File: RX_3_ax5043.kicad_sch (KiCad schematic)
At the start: 32 parts, among them U401 RFShield_OnePiece, U405 AX5043, U406 TPS22919D

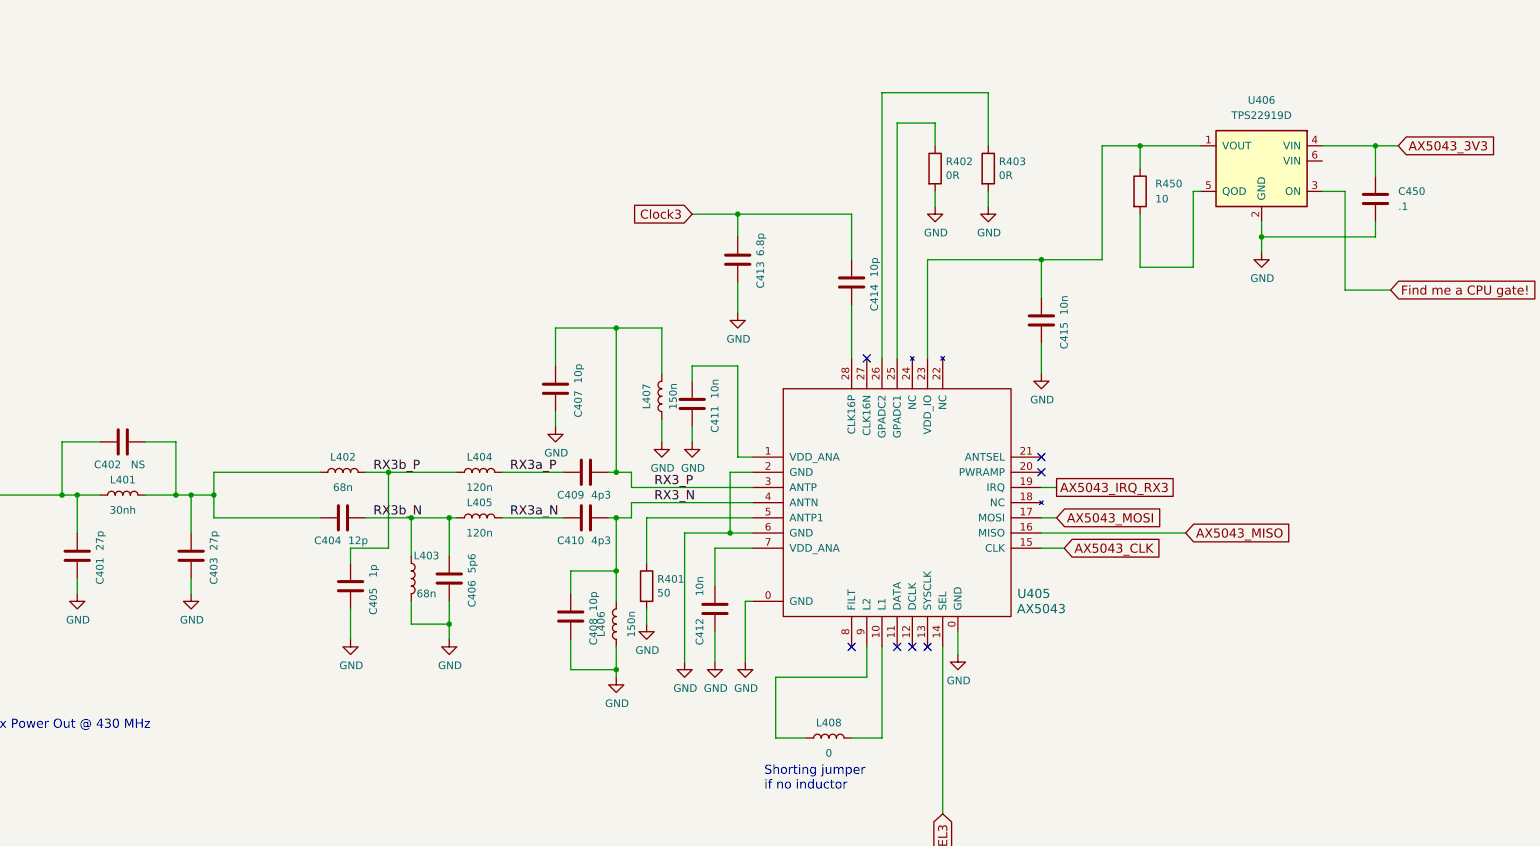
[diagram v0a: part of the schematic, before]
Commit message: Lots of cleanups to fix numerous issues
Signed-off-by: Corey Minyard <corey@minyard.net>
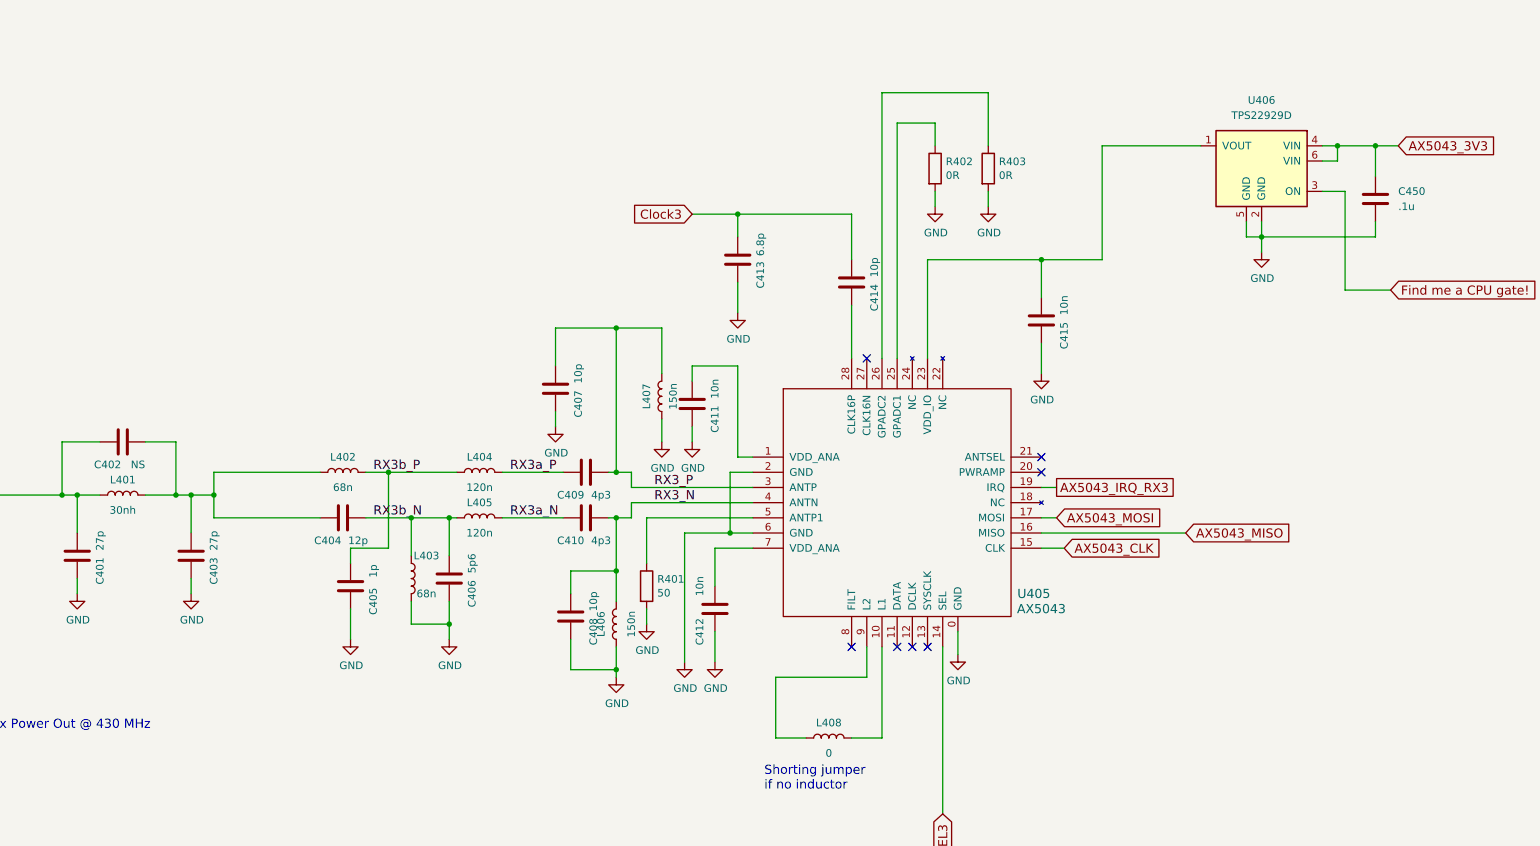
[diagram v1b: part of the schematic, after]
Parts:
- removed R450: 10, symbol Device:R
- C450: value .1 -> .1u; footprint (none) -> Capacitor_SMD:C_0402_1005Metric
- U406: value TPS22919D -> TPS22929D
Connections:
- net AX5043_3V3: now also U406.6 (VIN)
- net GND: now also U406.5 (GND)

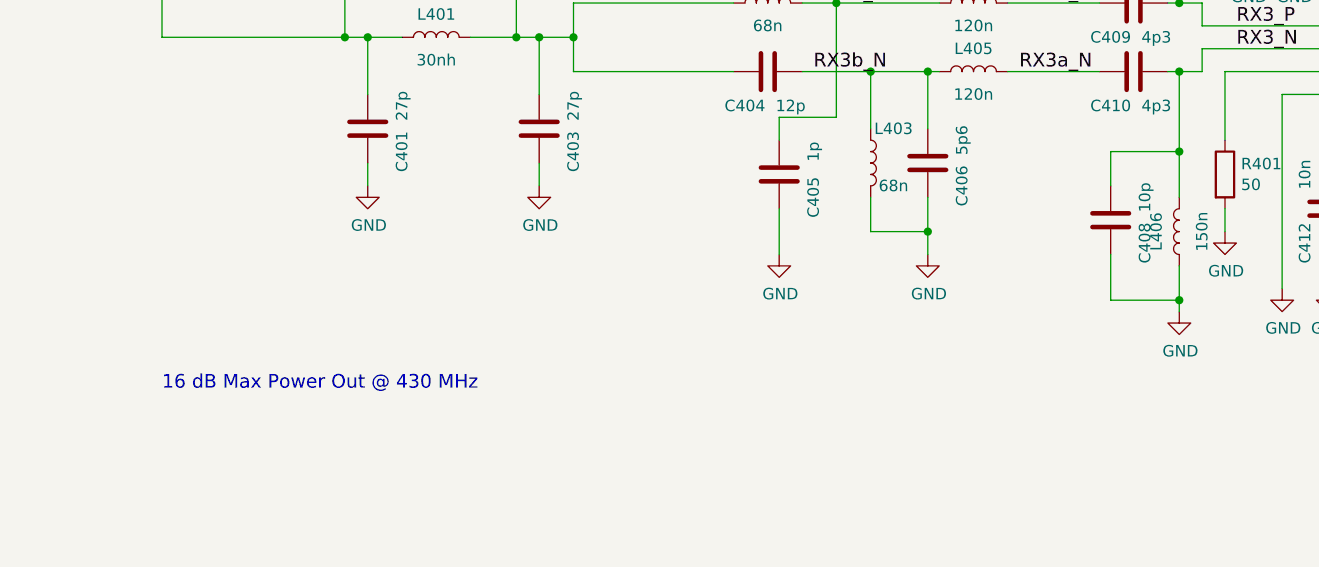
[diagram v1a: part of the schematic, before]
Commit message: Add notes file with todos and history, more cleanups
Signed-off-by: Corey Minyard <corey@minyard.net>
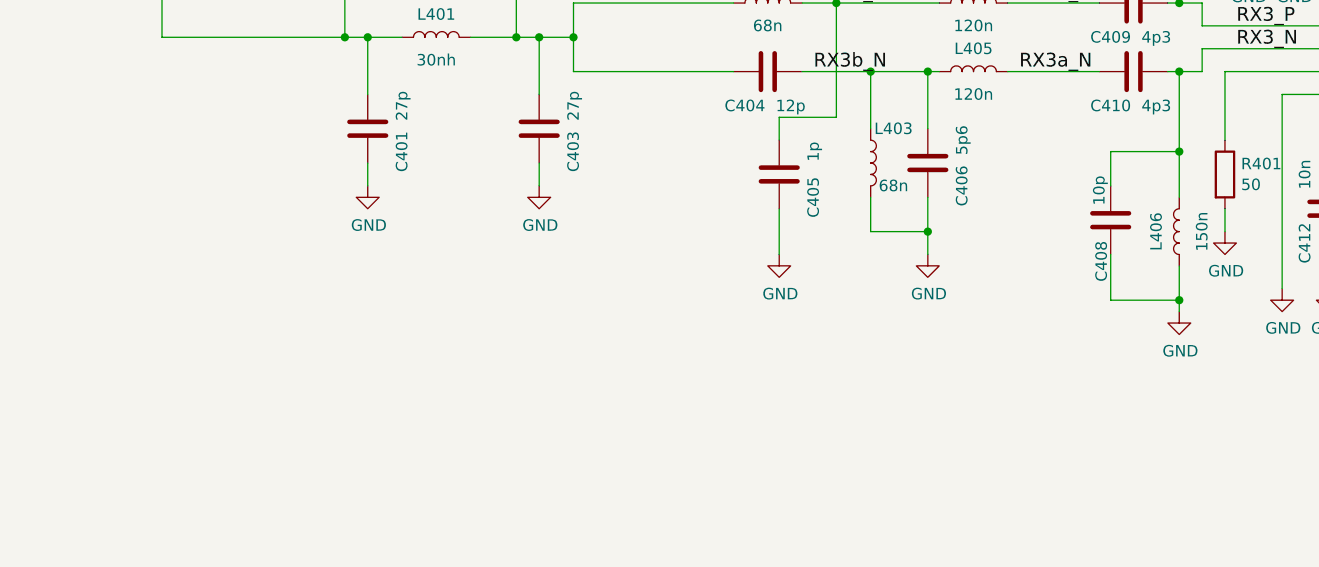
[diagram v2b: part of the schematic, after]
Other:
- note removed: "16 dB Max Power Out @ 430 MHz"
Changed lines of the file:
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@@
 		)
 	)
-	(text "16 dB Max Power Out @ 430 MHz"
-		(exclude_from_sim no)
-		(at 109.22 162.56 0)
-		(effects
-			(font
-				(size 1.524 1.524)
-			)
-			(justify left bottom)
-		)
-	)
 	(text "Symbol Numbers 400 up"
 		(exclude_from_sim no)
@@
 		(dnp no)
 		(property "Reference" "C408"
-			(at 218.44 146.05 90)
+			(at 213.614 148.082 90)
 			(effects
 				(font
@@
 		)
 		(property "Value" "10p"
-			(at 218.44 140.97 90)
+			(at 213.36 140.208 90)
 			(effects
 				(font

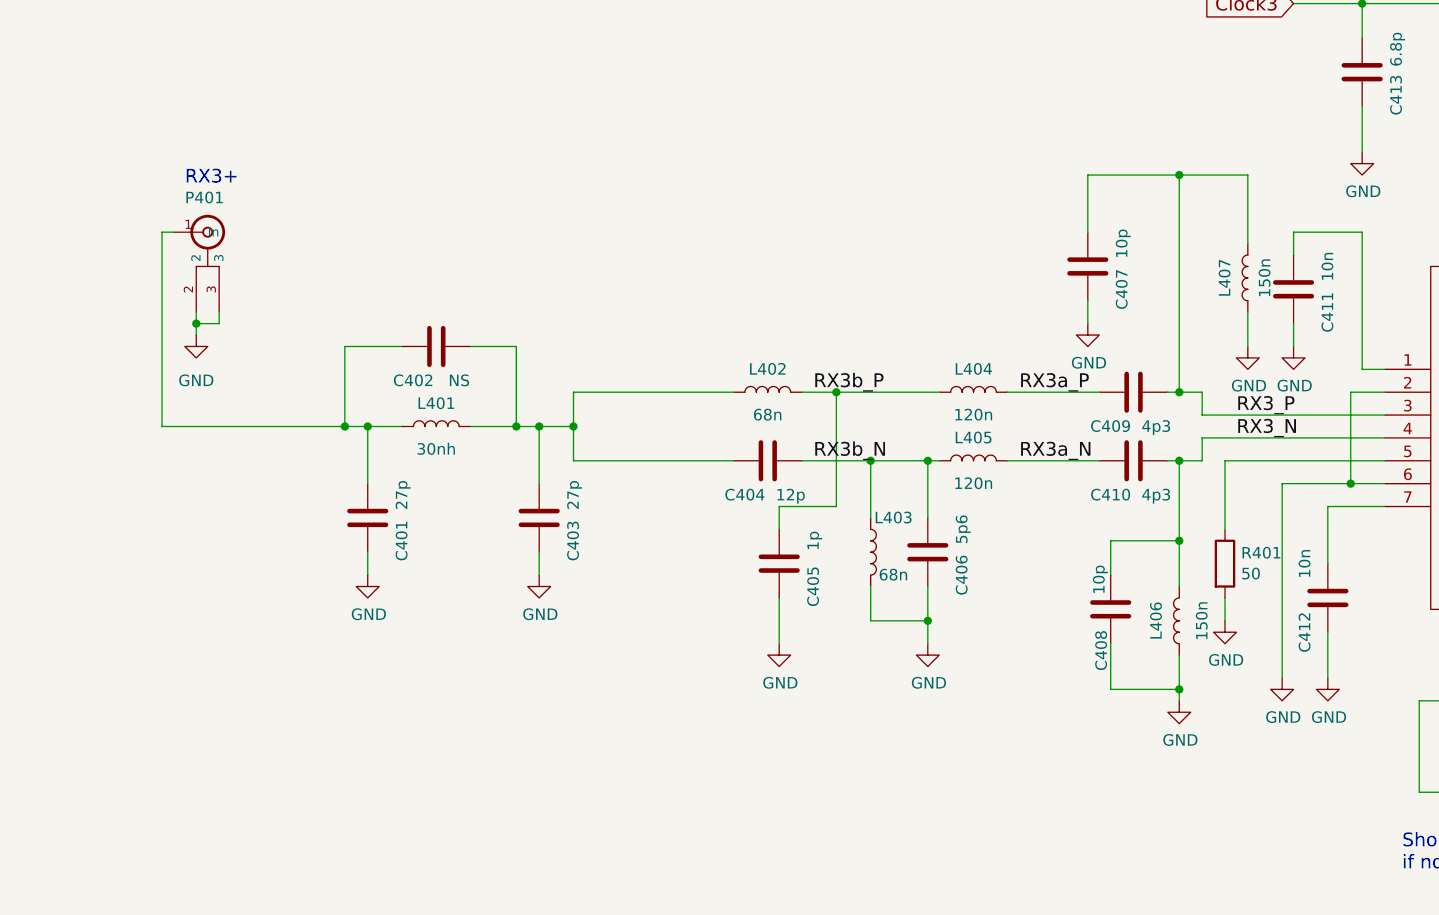
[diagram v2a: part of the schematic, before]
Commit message: Re-layout one ax5043 to reduce the size and add a balun
Signed-off-by: Corey Minyard <corey@minyard.net>
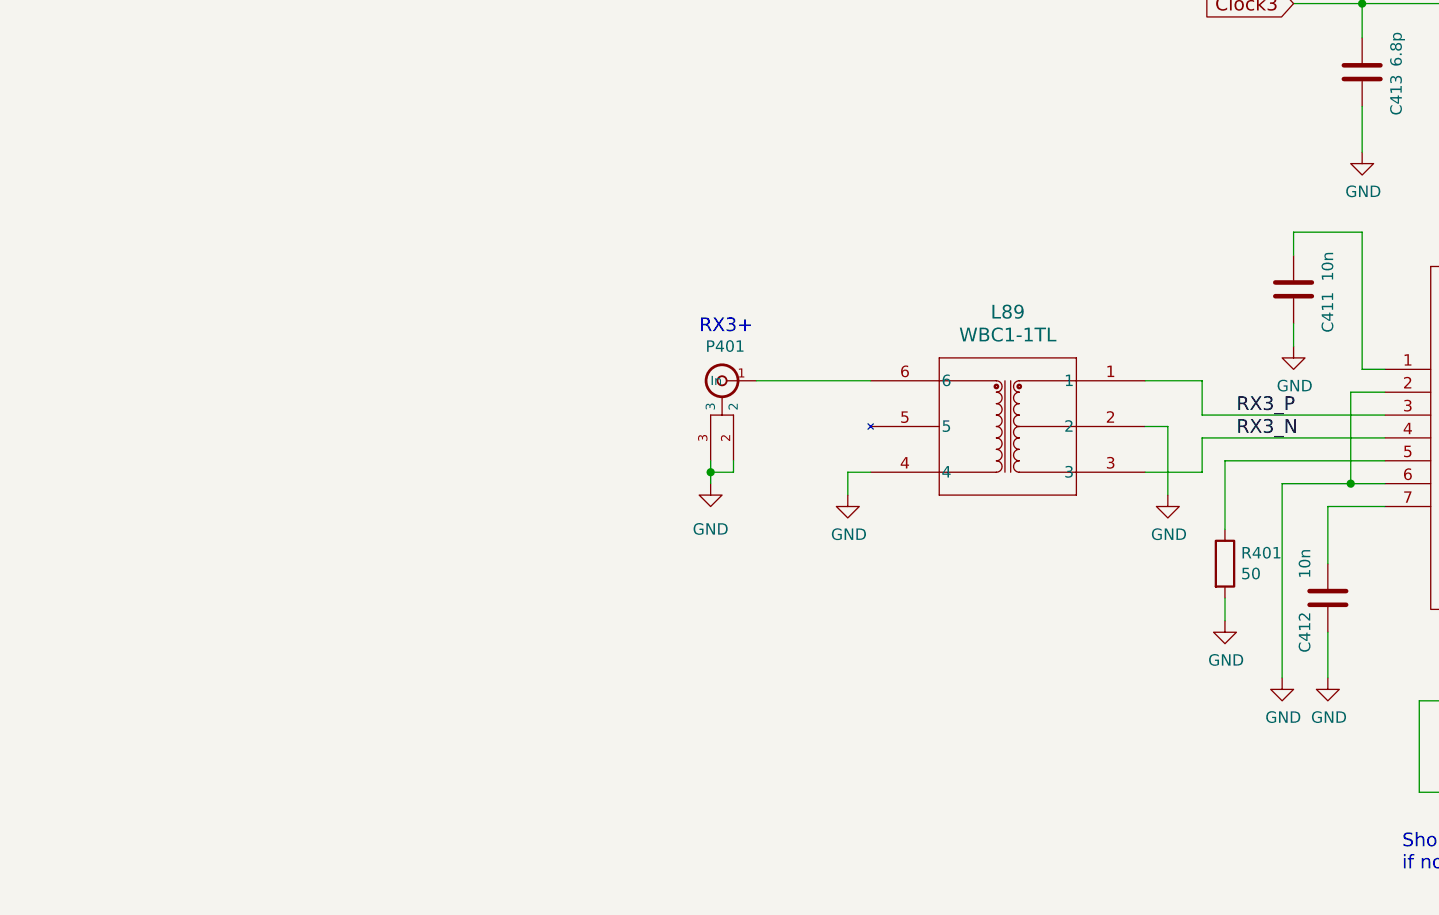
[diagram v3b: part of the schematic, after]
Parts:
- removed C401, C403: 27p, Capacitor_SMD:C_0603_1608Metric_Pad1.08x0.95mm_HandSolder, symbol Device:C
- removed C402: NS, Capacitor_SMD:C_0603_1608Metric_Pad1.08x0.95mm_HandSolder, symbol Device:C
- removed C404: 12p, Capacitor_SMD:C_0603_1608Metric_Pad1.08x0.95mm_HandSolder, symbol Device:C
- removed C405: 1p, Capacitor_SMD:C_0603_1608Metric_Pad1.08x0.95mm_HandSolder, symbol Device:C
- removed C406: 5p6, Capacitor_SMD:C_0603_1608Metric_Pad1.08x0.95mm_HandSolder, symbol Device:C
- removed C407, C408: 10p, Capacitor_SMD:C_0603_1608Metric_Pad1.08x0.95mm_HandSolder, symbol Device:C
- removed C409, C410: 4p3, Capacitor_SMD:C_0603_1608Metric_Pad1.08x0.95mm_HandSolder, symbol Device:C
- removed L401: 30nh, Inductor_SMD:L_0603_1608Metric_Pad1.05x0.95mm_HandSolder, symbol Device:L
- removed L402, L403: 68n, PacSatDev_misc:L_Murata_LQH2MCNxxxx02_2.0x1.6mm, symbol Device:L
- removed L404, L405: 120n, PacSatDev_misc:L_Murata_LQH2MCNxxxx02_2.0x1.6mm, symbol Device:L
- removed L406, L407: 150n, PacSatDev_misc:L_Murata_LQH2MCNxxxx02_2.0x1.6mm, symbol Device:L
- added L89: WBC1-1TL, IND6_WBC1, symbol PACSAT_DEV_misc:WBC1-1TL
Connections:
- net GND: now also L89.2, L89.4
- net RX3_N: now also L89.3
- net RX3_P: now also L89.1
- net at P401.1 (In): now also L89.6
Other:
- moved on the sheet: P401

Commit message: Start ripping things apart
Signed-off-by: Corey Minyard <corey@minyard.net>
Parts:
- added R88: 10K, Resistor_SMD:R_0603_1608Metric_Pad0.98x0.95mm_HandSolder, symbol Device:R
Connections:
- net GND: now also R88.2
- net Find me a CPU gate! renamed AX5043_EN_RX3
- net AX5043_EN_RX3: now also R88.1
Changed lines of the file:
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@@
+	)
+	(junction
+		(at 344.17 88.9)
+		(diameter 0)
+		(color 0 0 0 0)
 	)
 	(junction
@@
 	(wire
 		(pts
+			(xy 344.17 88.9) (xy 344.17 92.71)
+		)
+		(stroke
+			(width 0)
+			(type default)
+		)
+	)
+	(wire
+		(pts
 			(xy 266.7 148.59) (xy 266.7 163.83)
 		)
@@
 		(pts
 			(xy 293.37 132.08) (xy 297.18 132.08)
+		)
+		(stroke
+			(width 0)
+			(type default)
+		)
+	)
+	(wire
+		(pts
+			(xy 344.17 100.33) (xy 344.17 104.14)
 		)
 		(stroke
@@
 		)
 	)
-	(global_label "Find me a CPU gate!"
+	(global_label "AX5043_EN_RX3"
 		(shape input)
 		(at 351.79 88.9 0)
@@
 		)
 		(property "Intersheetrefs" "${INTERSHEET_REFS}"
-			(at 379.0435 88.9 0)
+			(at 372.8746 88.9 0)
 			(effects
 				(font
@@
 				(justify left)
 				(hide yes)
+			)
+		)
+	)
+	(symbol
+		(lib_id "Device:R")
+		(at 344.17 96.52 0)
+		(unit 1)
+		(exclude_from_sim no)
+		(in_bom yes)
+		(on_board yes)
+		(dnp no)
+		(property "Reference" "R88"
+			(at 337.82 95.25 0)
+			(effects
+				(font
+					(size 1.27 1.27)
+				)
+				(justify left)
+			)
+		)
+		(property "Value" "10K"
+			(at 336.55 97.79 0)
+			(effects
+				(font
+					(size 1.27 1.27)
+				)
+				(justify left)
+			)
+		)
+		(property "Footprint" "Resistor_SMD:R_0603_1608Metric_Pad0.98x0.95mm_HandSolder"
+			(at 342.392 96.52 90)
+			(effects
+				(font
+					(size 1.27 1.27)
+				)
+				(hide yes)
+			)
+		)
+		(property "Datasheet" "~"
+			(at 344.17 96.52 0)
+			(effects
+				(font
+					(size 1.27 1.27)
+				)
+			)
+		)
+		(property "Description" ""
+			(at 344.17 96.52 0)
+			(effects
+				(font
+					(size 1.27 1.27)
+				)
+			)
+		)
+		(pin "1"
+		)
+		(pin "2"
+		)
+		(instances
+			(project "PacSat_AFSK"
+				(path "/cc9f42d2-6985-41ac-acab-5ab7b01c5b38/9432d45f-be08-406b-8d9c-bfe62f690c2f"
+					(reference "R88")
+					(unit 1)
+				)
 			)
 		)
@@
 					(unit 1)
 				)
+			)
+		)
+	)
+	(symbol
+		(lib_id "power:GND")
+		(at 344.17 104.14 0)
+		(unit 1)
+		(exclude_from_sim no)
+		(in_bom yes)
+		(on_board yes)
+		(dnp no)
+		(property "Reference" "#PWR087"
+			(at 344.17 110.49 0)
+			(effects
+				(font
+					(size 1.27 1.27)
+				)
+				(hide yes)
+			)
+		)
+		(property "Value" "GND"
+			(at 344.297 108.5342 0)
+			(effects
+				(font
+					(size 1.27 1.27)
+				)
+			)
+		)
+		(property "Footprint" ""
+			(at 344.17 104.14 0)
+			(effects
+				(font
+					(size 1.27 1.27)
+				)
+				(hide yes)
+			)
+		)
+		(property "Datasheet" ""
+			(at 344.17 104.14 0)
+			(effects
+				(font
+					(size 1.27 1.27)
+				)
+				(hide yes)
+			)
+		)
+		(property "Description" ""
+			(at 344.17 104.14 0)
+			(effects
+				(font
+					(size 1.27 1.27)
+				)
+			)
+		)
+		(pin "1"
+		)
+		(instances
+			(project "PacSat_AFSK"
+				(path "/cc9f42d2-6985-41ac-acab-5ab7b01c5b38/9432d45f-be08-406b-8d9c-bfe62f690c2f"
+					(reference "#PWR087")
+					(unit 1)
+				)

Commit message: More hacking on things
Signed-off-by: Corey Minyard <corey@minyard.net>
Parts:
- removed U401: RFShield_OnePiece, PacSatDev_misc:RF_SHIELD_BMI_S_202_F_U401, symbol PACSAT_DEV_misc:RF_SHIELD_BOX
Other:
- note removed: "BMI_S_202_F"

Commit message: Clean up RTC, start working on power
Signed-off-by: Corey Minyard <corey@minyard.net>
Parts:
- L89: footprint IND6_WBC1 -> PacSatDev_misc:IND6_WBC1
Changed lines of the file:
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@@
 			)
 		)
-		(property "Footprint" "IND6_WBC1"
+		(property "Footprint" "PacSatDev_misc:IND6_WBC1"
 			(at 218.44 118.11 0)
 			(effects

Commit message: Finish up most of the ax5043 routing
Signed-off-by: Corey Minyard <corey@minyard.net>
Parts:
- L408: footprint PacSatDev_misc:L_Murata_LQH2MCNxxxx02_2.0x1.6mm -> Inductor_SMD:L_0603_1608Metric_Pad1.05x0.95mm_HandSolder
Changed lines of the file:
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@@
 			)
 		)
-		(property "Footprint" "PacSatDev_misc:L_Murata_LQH2MCNxxxx02_2.0x1.6mm"
+		(property "Footprint" "Inductor_SMD:L_0603_1608Metric_Pad1.05x0.95mm_HandSolder"
 			(at 257.81 163.83 0)
 			(effects
